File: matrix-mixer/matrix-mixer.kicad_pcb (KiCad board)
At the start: 2 copper layers, 58.4 x 44.4 mm, 2 parts, among them J1 PJ301M-12, J2 PJ301M-12

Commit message: matrix 0.0.1
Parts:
- removed J2: PJ301M-12, eurocad:PJ301M-12
- added C1: 4.7u, 4ms-footprints:Cap_Electrolytic_TH, F.Cu at (13.5, 97.8)
- added C2: 4.7u, 4ms-footprints:Cap_Electrolytic_TH, F.Cu at (36.3, 95.0)
- added D1: 1N4007, Diode_THT:D_DO-41_SOD81_P10.16mm_Horizontal, F.Cu at (6.10, 96.3)
- added D2: 1N4007, Diode_THT:D_DO-41_SOD81_P10.16mm_Horizontal, F.Cu at (43.9, 96.5)
- added IC1: LM324N, 4ms_Package_DIP:DIP-14_W7.62mm, F.Cu at (20.6, 83.3)
- added INPUT_A1: JACK-MONO, Eurocad:PJ301M-12, F.Cu at (-4.50, 0.95)
- added INPUT_B1: JACK_MONO, Eurocad:PJ301M-12, F.Cu at (-4.57, 20.1)
- added INPUT_C1: JACK_MONO, Eurocad:PJ301M-12, F.Cu at (-4.57, 39.4)
- added INPUT_D1: JACK_MONO, Eurocad:PJ301M-12, F.Cu at (-4.57, 58.7)
- added MUTE_A1: SW_SPST, 4ms-footprints:SPST-SUB, F.Cu at (-4.57, 11.2)
- added MUTE_B1: SW_SPST, 4ms-footprints:SPST-SUB, F.Cu at (-4.57, 30.5)
- added MUTE_C1: SW_SPST, 4ms-footprints:SPST-SUB, F.Cu at (-4.57, 49.8)
- added MUTE_D1: SW_SPST, 4ms-footprints:SPST-SUB, F.Cu at (-4.57, 69.1)
- added OUT_1: JACK-MONO, Eurocad:PJ301M-12, F.Cu at (6.10, 75.7)
- added OUT_2: JACK-MONO, Eurocad:PJ301M-12, F.Cu at (18.3, 75.7)
- added OUT_3: JACK-MONO, Eurocad:PJ301M-12, F.Cu at (30.5, 75.7)
- added OUT_4: JACK-MONO, Eurocad:PJ301M-12, F.Cu at (42.7, 75.9)
- added R1: 100k, Resistor_THT:R_Axial_DIN0207_L6.3mm_D2.5mm_P7.62mm_Horizontal, F.Cu at (2.03, 10.3)
- added R10: 100k, Resistor_THT:R_Axial_DIN0207_L6.3mm_D2.5mm_P7.62mm_Horizontal, F.Cu at (22.4, 49.3)
- added R11: 100k, Resistor_THT:R_Axial_DIN0207_L6.3mm_D2.5mm_P7.62mm_Horizontal, F.Cu at (26.7, 49.3)
- added R12: 100k, Resistor_THT:R_Axial_DIN0207_L6.3mm_D2.5mm_P7.62mm_Horizontal, F.Cu at (38.9, 49.3)
- added R13: 100k, Resistor_THT:R_Axial_DIN0207_L6.3mm_D2.5mm_P7.62mm_Horizontal, F.Cu at (2.29, 67.8)
- added R14: 100k, Resistor_THT:R_Axial_DIN0207_L6.3mm_D2.5mm_P7.62mm_Horizontal, F.Cu at (22.1, 67.8)
- added R15: 100k, Resistor_THT:R_Axial_DIN0207_L6.3mm_D2.5mm_P7.62mm_Horizontal, F.Cu at (26.4, 67.8)
- added R16: 100k, Resistor_THT:R_Axial_DIN0207_L6.3mm_D2.5mm_P7.62mm_Horizontal, F.Cu at (38.9, 67.8)
- added R2: 100k, Resistor_THT:R_Axial_DIN0207_L6.3mm_D2.5mm_P7.62mm_Horizontal, F.Cu at (22.4, 10.2)
- added R3: 100k, Resistor_THT:R_Axial_DIN0207_L6.3mm_D2.5mm_P7.62mm_Horizontal, F.Cu at (26.9, 10.2)
- added R4: 100k, Resistor_THT:R_Axial_DIN0207_L6.3mm_D2.5mm_P7.62mm_Horizontal, F.Cu at (38.4, 9.91)
- added R5: 100k, Resistor_THT:R_Axial_DIN0207_L6.3mm_D2.5mm_P7.62mm_Horizontal, F.Cu at (2.29, 29.7)
- added R6: 100k, Resistor_THT:R_Axial_DIN0207_L6.3mm_D2.5mm_P7.62mm_Horizontal, F.Cu at (22.4, 29.7)
- added R7: 100k, Resistor_THT:R_Axial_DIN0207_L6.3mm_D2.5mm_P7.62mm_Horizontal, F.Cu at (26.7, 29.7)
- added R8: 100k, Resistor_THT:R_Axial_DIN0207_L6.3mm_D2.5mm_P7.62mm_Horizontal, F.Cu at (38.9, 29.7)
- added R9: 100k, Resistor_THT:R_Axial_DIN0207_L6.3mm_D2.5mm_P7.62mm_Horizontal, F.Cu at (2.17, 49.4)
- added RV1: R_POT, 4ms-footprints:POT-9MM-ALPHA, F.Cu at (6.10, 0.25)
- added RV10: R_POT, 4ms-footprints:POT-9MM-ALPHA, F.Cu at (18.5, 38.6)
- added RV11: R_POT, 4ms-footprints:POT-9MM-ALPHA, F.Cu at (30.7, 38.6)
- added RV12: R_POT, 4ms-footprints:POT-9MM-ALPHA, F.Cu at (42.9, 38.6)
- added RV13: R_POT, 4ms-footprints:POT-9MM-ALPHA, F.Cu at (6.10, 57.8)
- added RV14: R_POT, 4ms-footprints:POT-9MM-ALPHA, F.Cu at (18.3, 57.9)
- added RV15: R_POT, 4ms-footprints:POT-9MM-ALPHA, F.Cu at (30.5, 57.9)
- added RV16: R_POT, 4ms-footprints:POT-9MM-ALPHA, F.Cu at (42.7, 57.9)
- added RV2: R_POT, 4ms-footprints:POT-9MM-ALPHA, F.Cu at (18.3, 0.25)
- added RV3: R_POT, 4ms-footprints:POT-9MM-ALPHA, F.Cu at (30.5, 0.30)
- added RV4: R_POT, 4ms-footprints:POT-9MM-ALPHA, F.Cu at (42.7, 0.32)
- added RV5: R_POT, 4ms-footprints:POT-9MM-ALPHA, F.Cu at (6.10, 19.3)
- added RV6: R_POT, 4ms-footprints:POT-9MM-ALPHA, F.Cu at (18.3, 19.3)
- added RV7: R_POT, 4ms-footprints:POT-9MM-ALPHA, F.Cu at (30.5, 19.3)
- added RV8: R_POT, 4ms-footprints:POT-9MM-ALPHA, F.Cu at (42.7, 19.3)
- added RV9: R_POT, 4ms-footprints:POT-9MM-ALPHA, F.Cu at (6.35, 38.6)
- J1: value PJ301M-12 -> EURO_HEADER_10pin; footprint eurocad:PJ301M-12 -> 4ms-footprints:Header_2x05_Pitch2.54mm_TH_-12v_Label
- moved J1 123.1 mm to (-2.03, 99.3)
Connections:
- J1 pad 1: Earth -> Net-(D1-Pad2)
- J1 pad 3: Net-(J1-Pad3) -> GND
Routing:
- net Net-(IC1-Pad5): track 0.00 -> 95.7 mm
- net Net-(IC1-Pad10): track 0.00 -> 94.0 mm
- net Net-(IC1-Pad12): track 0.00 -> 84.4 mm
- net Net-(IC1-Pad3): track 0.00 -> 83.5 mm
- net Net-(D2-Pad1): track 0.00 -> 55.5 mm
- net Net-(MUTE_C1-Pad2): track 0.00 -> 48.2 mm
- net Net-(MUTE_D1-Pad2): track 0.00 -> 48.0 mm
- net Net-(MUTE_A1-Pad2): track 0.00 -> 47.7 mm
- net Net-(MUTE_B1-Pad2): track 0.00 -> 47.7 mm
- net Net-(J1-Pad2): track 32.3 -> 0.00 mm
- net Net-(J1-Pad3): track 32.3 -> 0.00 mm
- net /VEE: track 0.00 -> 25.2 mm
- net Net-(IC1-Pad6): track 0.00 -> 23.7 mm
- net Net-(IC1-Pad8): track 0.00 -> 23.0 mm
- net /VCC: track 0.00 -> 19.3 mm
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- added copper zone on F.Cu, net GND
- removed copper zone on B.Cu, net Earth
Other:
- board size 58.4 x 44.4 mm -> 58.4 x 108 mm
- board text added: "Matrix Mixer 0.0.1"
- board text added: "Paul Adenot"
- board text removed: "Je suis un grand poney"
- board text removed: "Un très grand poney"

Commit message: version sent to fab
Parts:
- moved OUT_4 37.5 mm to (72.6, 98.6)
- moved C2 37.5 mm to (66.3, 117.6)
- moved D2 37.5 mm to (73.9, 119.1)
- moved J1 37.5 mm to (27.9, 121.9)
- moved R11 37.5 mm to (56.6, 71.9)
- moved R12 37.5 mm to (68.8, 71.9)
- moved R13 37.5 mm to (32.3, 90.4)
- moved R14 37.5 mm to (52.1, 90.4)
- moved R16 37.5 mm to (68.8, 90.4)
- moved R9 37.5 mm to (32.1, 72.0)
- moved RV10 37.5 mm to (48.5, 61.2)
- moved RV11 37.5 mm to (60.7, 61.2)
- moved RV16 37.5 mm to (72.6, 80.5)
- moved RV4 37.5 mm to (72.6, 22.9)
- moved RV8 37.5 mm to (72.6, 41.9)
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
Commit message: matrix 0.0.2 but not routed
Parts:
- removed MUTE_A1, MUTE_B1, MUTE_C1, MUTE_D1: SW_SPST, 4ms-footprints:SPST-SUB
- added IC2: LM324N, 4ms_Package_DIP:DIP-14_W7.62mm, F.Cu at (64.3, 104.6)
- added R17: 70k, 4ms_Resistor:R_Axial_DIN0207_L6.3mm_D2.5mm_P7.62mm_Horizontal, F.Cu at (36.6, 115.3)
- added R18: 100k, 4ms_Resistor:R_Axial_DIN0207_L6.3mm_D2.5mm_P7.62mm_Horizontal, F.Cu at (33.8, 115.3)
- added R19: 100k, 4ms_Resistor:R_Axial_DIN0207_L6.3mm_D2.5mm_P7.62mm_Horizontal, F.Cu at (30.7, 122.9)
- added R20: 70k, 4ms_Resistor:R_Axial_DIN0207_L6.3mm_D2.5mm_P7.62mm_Horizontal, F.Cu at (52.1, 118.9)
- added R21: 100k, 4ms_Resistor:R_Axial_DIN0207_L6.3mm_D2.5mm_P7.62mm_Horizontal, F.Cu at (55.1, 115.3)
- added R22: 100k, 4ms_Resistor:R_Axial_DIN0207_L6.3mm_D2.5mm_P7.62mm_Horizontal, F.Cu at (52.1, 106.7)
- added R23: 70k, 4ms_Resistor:R_Axial_DIN0207_L6.3mm_D2.5mm_P7.62mm_Horizontal, F.Cu at (57.9, 106.2)
- added R24: 100k, 4ms_Resistor:R_Axial_DIN0207_L6.3mm_D2.5mm_P7.62mm_Horizontal, F.Cu at (61.0, 113.0)
- added R25: 100k, 4ms_Resistor:R_Axial_DIN0207_L6.3mm_D2.5mm_P7.62mm_Horizontal, F.Cu at (58.9, 122.9)
- added R26: 70k, 4ms_Resistor:R_Axial_DIN0207_L6.3mm_D2.5mm_P7.62mm_Horizontal, F.Cu at (73.2, 123.2)
- added R27: 100k, 4ms_Resistor:R_Axial_DIN0207_L6.3mm_D2.5mm_P7.62mm_Horizontal, F.Cu at (74.7, 112.3)
- added R28: 100k, 4ms_Resistor:R_Axial_DIN0207_L6.3mm_D2.5mm_P7.62mm_Horizontal, F.Cu at (77.2, 107.7)
- moved D2 51.9 mm to (22.9, 110.0), turned to 270 degrees
- moved C2 38.8 mm to (28.2, 110.2)
- moved J1 16.8 mm to (27.7, 105.2)
- moved D1 15.7 mm to (29.5, 104.6)
- moved C1 15.3 mm to (35.3, 107.4)
- moved IC1 9.23 mm to (41.4, 104.6)
- moved INPUT_D1 4.83 mm to (25.4, 76.5)
- moved R13 4.83 mm to (32.3, 85.6)
- moved R14 4.83 mm to (52.1, 85.6)
- moved R15 4.83 mm to (56.4, 85.6)
- moved R16 4.83 mm to (68.8, 85.6)
- moved RV13 4.83 mm to (36.1, 75.6)
- moved RV14 4.83 mm to (48.3, 75.7)
- moved RV15 4.83 mm to (60.5, 75.7)
- moved RV16 4.83 mm to (72.6, 75.7)
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- renumbered OUT_1 to OUTPUT_A1, OUT_2 to OUTPUT_B1, OUT_3 to OUTPUT_C1, OUT_4 to OUTPUT_D1
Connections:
- IC1 pad 10: Net-(IC1-Pad10) -> GND
- IC1 pad 12: Net-(IC1-Pad12) -> GND
- IC1 pad 14: Net-(IC1-Pad13) -> Net-(IC1-Pad14)
- IC1 pad 2: Net-(IC1-Pad1) -> Net-(IC1-Pad2)
- IC1 pad 3: Net-(IC1-Pad3) -> GND
- IC1 pad 5: Net-(IC1-Pad5) -> GND
- IC1 pad 7: Net-(IC1-Pad6) -> Net-(IC1-Pad7)
- IC1 pad 9: Net-(IC1-Pad8) -> Net-(IC1-Pad9)
- INPUT_A1 pad 1: Net-(INPUT_A1-Pad1) -> (no net)
- INPUT_B1 pad 1: Net-(INPUT_B1-Pad1) -> (no net)
- INPUT_C1 pad 1: Net-(INPUT_C1-Pad1) -> (no net)
- INPUT_D1 pad 1: Net-(INPUT_D1-Pad1) -> (no net)
- J1 pad 10: Net-(J1-Pad10) -> (no net)
- J1 pad 2: Net-(J1-Pad2) -> (no net)
- OUTPUT_A1 pad 1: Net-(IC1-Pad6) -> (no net)
- OUTPUT_A1 pad 3: Net-(J2-Pad3) -> Net-(IC1-Pad7)
- OUTPUT_B1 pad 1: Net-(IC1-Pad1) -> (no net)
- OUTPUT_B1 pad 3: Net-(J3-Pad3) -> Net-(IC1-Pad14)
- OUTPUT_C1 pad 1: Net-(IC1-Pad13) -> (no net)
- OUTPUT_D1 pad 1: Net-(IC1-Pad8) -> (no net)
- R1 pad 2: Net-(IC1-Pad5) -> Net-(IC1-Pad2)
- R10 pad 2: Net-(IC1-Pad3) -> Net-(IC1-Pad9)
- R11 pad 2: Net-(IC1-Pad12) -> Net-(IC2-Pad2)
- R12 pad 2: Net-(IC1-Pad10) -> Net-(IC2-Pad9)
- R13 pad 2: Net-(IC1-Pad5) -> Net-(IC1-Pad2)
- R14 pad 2: Net-(IC1-Pad3) -> Net-(IC1-Pad9)
- R15 pad 2: Net-(IC1-Pad12) -> Net-(IC2-Pad2)
- R16 pad 2: Net-(IC1-Pad10) -> Net-(IC2-Pad9)
- R2 pad 2: Net-(IC1-Pad3) -> Net-(IC1-Pad9)
- R3 pad 2: Net-(IC1-Pad12) -> Net-(IC2-Pad2)
- R4 pad 2: Net-(IC1-Pad10) -> Net-(IC2-Pad9)
- R5 pad 2: Net-(IC1-Pad5) -> Net-(IC1-Pad2)
- R6 pad 2: Net-(IC1-Pad3) -> Net-(IC1-Pad9)
- R7 pad 2: Net-(IC1-Pad12) -> Net-(IC2-Pad2)
- R8 pad 2: Net-(IC1-Pad10) -> Net-(IC2-Pad9)
- R9 pad 2: Net-(IC1-Pad5) -> Net-(IC1-Pad2)
- RV1 pad 1: Net-(MUTE_A1-Pad2) -> GND
- RV1 pad 3: GND -> Net-(INPUT_A1-Pad3)
- RV10 pad 1: Net-(MUTE_C1-Pad2) -> GND
- RV10 pad 3: GND -> Net-(INPUT_C1-Pad3)
- RV11 pad 1: Net-(MUTE_C1-Pad2) -> GND
- RV11 pad 3: GND -> Net-(INPUT_C1-Pad3)
- RV12 pad 1: Net-(MUTE_C1-Pad2) -> GND
- RV12 pad 3: GND -> Net-(INPUT_C1-Pad3)
- RV13 pad 1: Net-(MUTE_D1-Pad2) -> GND
- RV13 pad 3: GND -> Net-(INPUT_D1-Pad3)
- RV14 pad 1: Net-(MUTE_D1-Pad2) -> GND
- RV14 pad 3: GND -> Net-(INPUT_D1-Pad3)
- RV15 pad 1: Net-(MUTE_D1-Pad2) -> GND
- RV15 pad 3: GND -> Net-(INPUT_D1-Pad3)
- RV16 pad 1: Net-(MUTE_D1-Pad2) -> GND
- RV16 pad 3: GND -> Net-(INPUT_D1-Pad3)
- RV2 pad 1: Net-(MUTE_A1-Pad2) -> GND
- RV2 pad 3: GND -> Net-(INPUT_A1-Pad3)
- RV3 pad 1: Net-(MUTE_A1-Pad2) -> GND
- RV3 pad 3: GND -> Net-(INPUT_A1-Pad3)
- RV4 pad 1: Net-(MUTE_A1-Pad2) -> GND
- RV4 pad 3: GND -> Net-(INPUT_A1-Pad3)
- RV5 pad 1: Net-(MUTE_B1-Pad2) -> GND
- RV5 pad 3: GND -> Net-(INPUT_B1-Pad3)
- RV6 pad 1: Net-(MUTE_B1-Pad2) -> GND
- RV6 pad 3: GND -> Net-(INPUT_B1-Pad3)
- RV7 pad 1: Net-(MUTE_B1-Pad2) -> GND
- RV7 pad 3: GND -> Net-(INPUT_B1-Pad3)
- RV8 pad 1: Net-(MUTE_B1-Pad2) -> GND
- RV8 pad 3: GND -> Net-(INPUT_B1-Pad3)
- RV9 pad 1: Net-(MUTE_C1-Pad2) -> GND
- RV9 pad 3: GND -> Net-(INPUT_C1-Pad3)
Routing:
- net Net-(IC1-Pad5): track 95.7 -> 0.00 mm
- net Net-(IC1-Pad10): track 94.0 -> 0.00 mm
- net Net-(IC1-Pad12): track 84.4 -> 0.00 mm
- net Net-(IC1-Pad3): track 83.5 -> 0.00 mm
- net Net-(D2-Pad1): track 55.5 -> 0.00 mm
- net Net-(MUTE_C1-Pad2): track 48.2 -> 0.00 mm
- net Net-(MUTE_D1-Pad2): track 48.0 -> 0.00 mm
- net Net-(MUTE_A1-Pad2): track 47.7 -> 0.00 mm
- net Net-(MUTE_B1-Pad2): track 47.7 -> 0.00 mm
- net /VEE: track 25.2 -> 0.00 mm
- net Net-(IC1-Pad6): track 23.7 -> 0.00 mm
- net Net-(IC1-Pad8): track 23.0 -> 0.00 mm
- net /VCC: track 19.3 -> 0.00 mm
- net Net-(INPUT_D1-Pad3): track 16.4 -> 0.00 mm
- net Net-(INPUT_C1-Pad3): track 16.4 -> 0.00 mm
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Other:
- board text added: "Matrix Mixer 0.0.2"
- board text removed: "Matrix Mixer 0.0.1"

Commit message: matrix mixer 0.0.2 routed ready to send
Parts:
- removed INPUT_A1, OUTPUT_A1, OUTPUT_B1, OUTPUT_C1, OUTPUT_D1: JACK-MONO, Eurocad:PJ301M-12
- removed INPUT_B1, INPUT_C1, INPUT_D1: JACK_MONO, Eurocad:PJ301M-12
- added INPUT_A: THONKICONNNEW, Connector_Audio:Jack_3.5mm_QingPu_WQP-PJ398SM_Vertical_CircularHoles, F.Cu at (26.2, 31.0)
- added INPUT_B: THONKICONNNEW, Connector_Audio:Jack_3.5mm_QingPu_WQP-PJ398SM_Vertical_CircularHoles, F.Cu at (25.9, 48.0)
- added INPUT_C: THONKICONNNEW, Connector_Audio:Jack_3.5mm_QingPu_WQP-PJ398SM_Vertical_CircularHoles, F.Cu at (25.9, 65.3)
- added INPUT_D: THONKICONNNEW, Connector_Audio:Jack_3.5mm_QingPu_WQP-PJ398SM_Vertical_CircularHoles, F.Cu at (25.7, 82.5)
- added OUTPUT_A: THONKICONNNEW, Connector_Audio:Jack_3.5mm_QingPu_WQP-PJ398SM_Vertical_CircularHoles, F.Cu at (36.5, 88.9)
- added OUTPUT_B: THONKICONNNEW, Connector_Audio:Jack_3.5mm_QingPu_WQP-PJ398SM_Vertical_CircularHoles, F.Cu at (48.3, 88.9)
- added OUTPUT_C: THONKICONNNEW, Connector_Audio:Jack_3.5mm_QingPu_WQP-PJ398SM_Vertical_CircularHoles, F.Cu at (60.5, 88.9)
- added OUTPUT_D: THONKICONNNEW, Connector_Audio:Jack_3.5mm_QingPu_WQP-PJ398SM_Vertical_CircularHoles, F.Cu at (72.6, 89.2)
- moved R25 15.5 mm to (61.7, 107.7), turned to 90 degrees
- moved R23 12.5 mm to (61.7, 118.1), turned to 270 degrees
- moved R19 9.20 mm to (35.1, 114.8), turned to 90 degrees
- moved R2 7.98 mm to (44.5, 34.0), turned to 0 degrees
- moved R6 7.94 mm to (44.5, 51.3), turned to 0 degrees
- moved R14 7.62 mm to (44.5, 85.9), turned to 0 degrees
- moved R10 7.41 mm to (44.7, 68.6), turned to 0 degrees
- moved R17 7.13 mm to (37.1, 122.4), turned to 180 degrees
- moved R27 6.04 mm to (77.0, 117.9)
- moved R26 5.48 mm to (74.4, 117.9), turned to 270 degrees
- moved R24 5.38 mm to (59.2, 118.1), turned to 90 degrees
- moved R18 4.35 mm to (38.1, 114.8), turned to 90 degrees
- moved R21 2.81 mm to (54.9, 118.1)
- moved R28 2.81 mm to (74.4, 107.4)
- moved C1 2.27 mm to (34.3, 105.4), turned to 0 degrees
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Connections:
- J1 pad 10: (no net) -> Net-(D2-Pad1)
- J1 pad 2: (no net) -> Net-(D1-Pad2)
- R1 pad 2: Net-(IC1-Pad2) -> Net-(IC1-Pad6)
- R11 pad 2: Net-(IC2-Pad2) -> Net-(IC2-Pad6)
- R13 pad 2: Net-(IC1-Pad2) -> Net-(IC1-Pad6)
- R15 pad 2: Net-(IC2-Pad2) -> Net-(IC2-Pad6)
- R17 pad 1: Net-(IC1-Pad2) -> Net-(IC1-Pad6)
- R17 pad 2: Net-(IC1-Pad1) -> Net-(IC1-Pad7)
- R18 pad 1: Net-(IC1-Pad1) -> Net-(IC1-Pad7)
- R18 pad 2: Net-(IC1-Pad6) -> Net-(IC1-Pad2)
- R19 pad 1: Net-(IC1-Pad6) -> Net-(IC1-Pad2)
- R19 pad 2: Net-(IC1-Pad7) -> Net-(IC1-Pad1)
- R23 pad 1: Net-(IC2-Pad2) -> Net-(IC2-Pad6)
- R23 pad 2: Net-(IC2-Pad1) -> Net-(IC2-Pad7)
- R24 pad 1: Net-(IC2-Pad1) -> Net-(IC2-Pad7)
- R24 pad 2: Net-(IC2-Pad6) -> Net-(IC2-Pad2)
- R25 pad 1: Net-(IC2-Pad6) -> Net-(IC2-Pad2)
- R25 pad 2: Net-(IC2-Pad7) -> Net-(IC2-Pad1)
- R3 pad 2: Net-(IC2-Pad2) -> Net-(IC2-Pad6)
- R5 pad 2: Net-(IC1-Pad2) -> Net-(IC1-Pad6)
- R7 pad 2: Net-(IC2-Pad2) -> Net-(IC2-Pad6)
- R9 pad 2: Net-(IC1-Pad2) -> Net-(IC1-Pad6)
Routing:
- net Net-(IC1-Pad6): track 0.00 -> 94.1 mm
- net Net-(IC1-Pad9): track 0.00 -> 94.1 mm
- net Net-(IC2-Pad9): track 0.00 -> 93.5 mm
- net Net-(IC2-Pad6): track 0.00 -> 90.6 mm
- net Net-(INPUT_C1-PadP$1_TIP): track 0.00 -> 58.3 mm
- net Net-(INPUT_B1-PadP$1_TIP): track 0.00 -> 58.1 mm
- net Net-(INPUT_D1-PadP$1_TIP): track 0.00 -> 58.0 mm
- net /VEE: track 0.00 -> 57.9 mm
- net Net-(INPUT_A1-PadP$1_TIP): track 0.00 -> 57.9 mm
- net /VCC: track 0.00 -> 48.2 mm
- net GND: track 0.00 -> 22.9 mm
- net Net-(IC1-Pad1): track 0.00 -> 16.2 mm
- net Net-(IC1-Pad2): track 0.00 -> 14.9 mm
- net Net-(IC1-Pad13): track 0.00 -> 10.5 mm
- net Net-(IC2-Pad2): track 0.00 -> 10.0 mm
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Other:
- board text added: "Swap VEE conditioning line with 10pin connector to be able to bend cap ?"

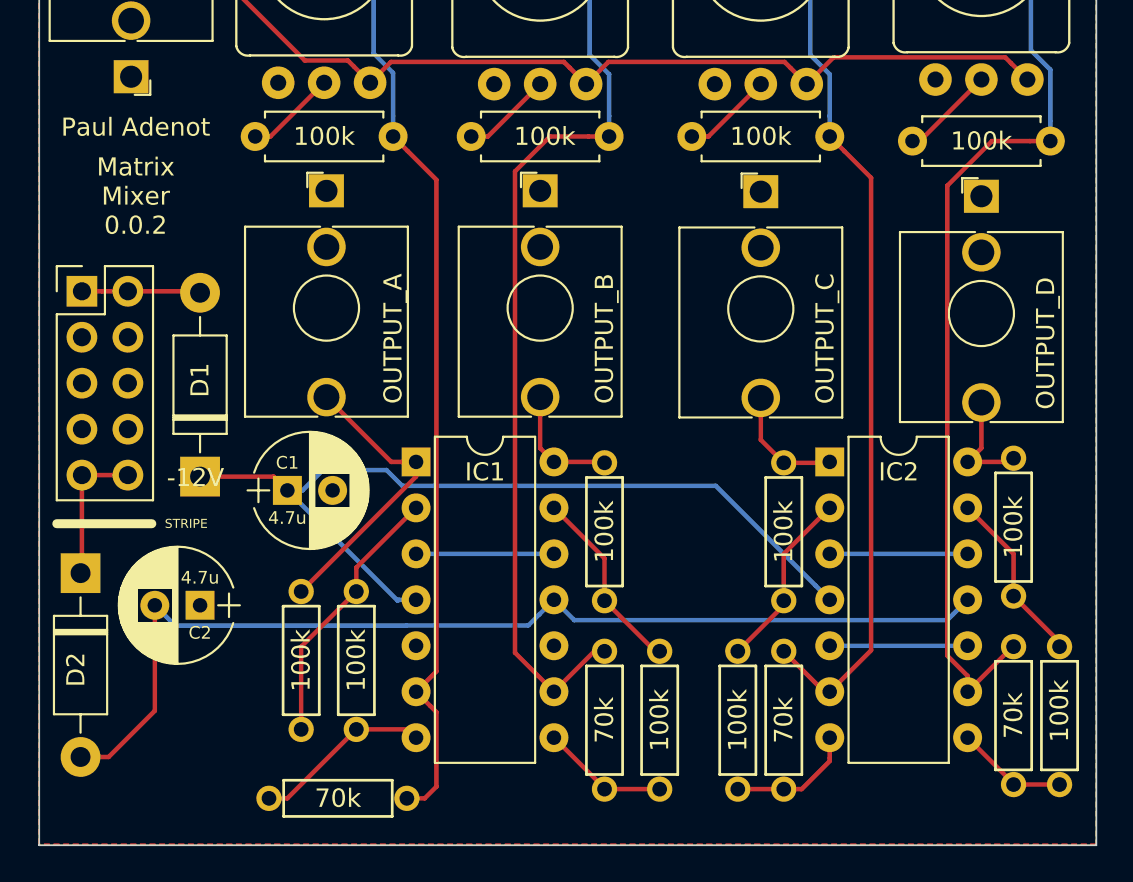
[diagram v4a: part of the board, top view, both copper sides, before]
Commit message: matrix mixer: svg face plate at scale + re-save board file
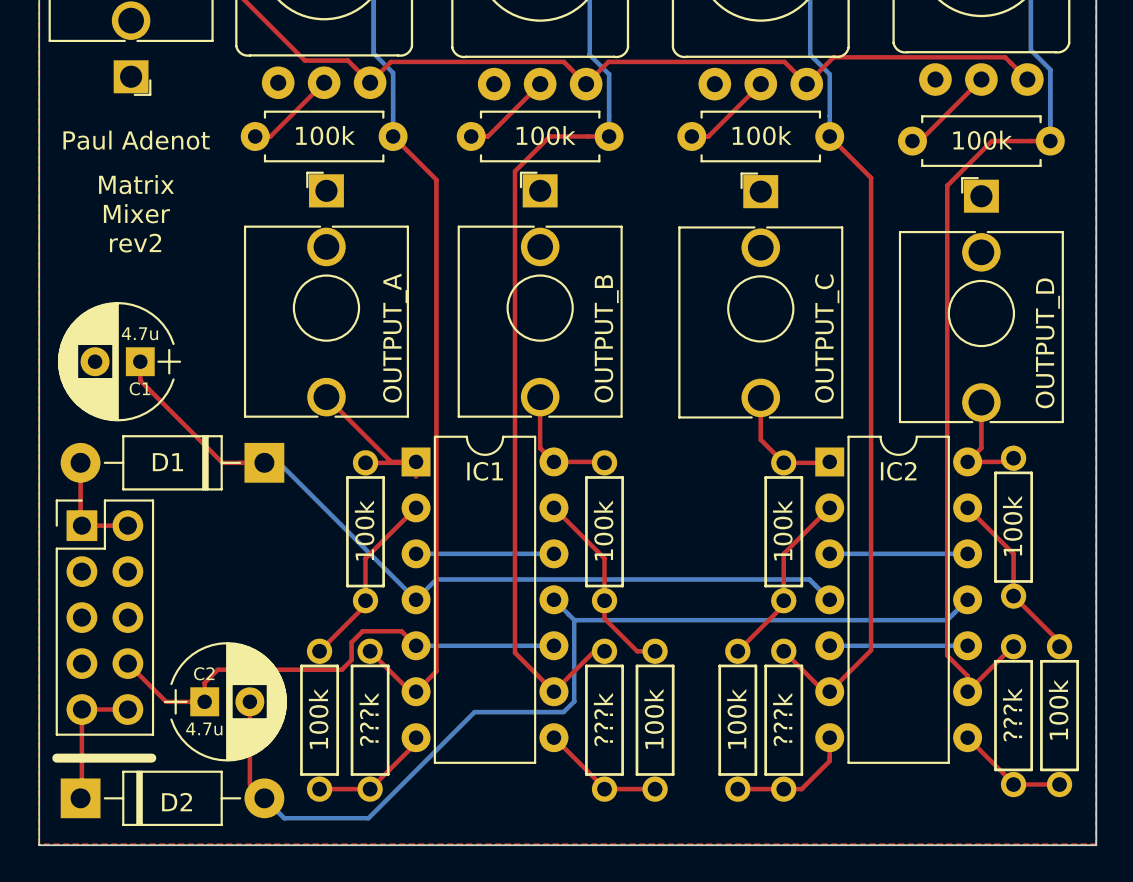
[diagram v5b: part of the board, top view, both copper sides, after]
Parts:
- R17, R20, R23, R26: value 70k -> ???k
- moved J1 13.0 mm to (27.7, 118.1)
- moved D2 12.4 mm to (22.9, 122.4), turned to 0 degrees
- moved C1 10.8 mm to (26.2, 98.3), turned to 180 degrees
- moved R19 7.95 mm to (38.6, 107.7)
- moved C2 5.34 mm to (29.7, 117.1), turned to 0 degrees
- moved R17 4.67 mm to (38.9, 118.1), turned to 270 degrees
- moved R18 3.88 mm to (36.1, 118.1)
- moved D1 3.64 mm to (33.0, 103.9), turned to 180 degrees
- moved R21 0.25 mm to (54.6, 118.1)
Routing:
- net GND: track 22.9 -> 50.4 mm
- net Net-(IC1-Pad1): track 16.2 -> 10.1 mm
- net Net-(IC1-Pad2): track 14.9 -> 10.1 mm
- net Net-(IC1-Pad6): track 94.1 -> 90.0 mm
- net /VEE: track 57.9 -> 54.2 mm
- net /VCC: track 48.2 -> 45.1 mm
- net Net-(IC1-Pad7): track 9.90 -> 7.34 mm
- net Net-(IC1-Pad13): track 10.5 -> 11.1 mm
- net Net-(D1-Pad2): track 6.56 -> 6.05 mm
- net Net-(D2-Pad1): track 7.99 -> 7.48 mm
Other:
- board text added: "Matrix Mixer rev2"
- board text removed: "Matrix Mixer 0.0.2"
- board text removed: "Swap VEE conditioning line with 10pin connector to be able to bend cap ?"
